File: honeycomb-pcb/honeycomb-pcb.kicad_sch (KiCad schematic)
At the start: 0 parts

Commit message: tmc5130-uart-multiplexer -> honeycomb-pcb
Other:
- title: tmc5130-uart-multiplexer -> honeycomb-pcb
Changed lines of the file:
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@@
   (paper "A4")
   (title_block
-    (title "tmc5130-uart-multiplexer")
+    (title "honeycomb-pcb")
     (date "2024-07-10")
     (rev "1.0")
@@
     )
     (instances
-      (project "tmc5130-uart-multiplexer"
+      (project "honeycomb-pcb"
         (path "/df2b2e89-e055-4140-95de-f1df723db034" (page "2"))
       )
@@
     )
     (instances
-      (project "tmc5130-uart-multiplexer"
+      (project "honeycomb-pcb"
         (path "/df2b2e89-e055-4140-95de-f1df723db034" (page "5"))
       )
@@
     )
     (instances
-      (project "tmc5130-uart-multiplexer"
+      (project "honeycomb-pcb"
         (path "/df2b2e89-e055-4140-95de-f1df723db034" (page "9"))
       )
@@
     )
     (instances
-      (project "tmc5130-uart-multiplexer"
+      (project "honeycomb-pcb"
         (path "/df2b2e89-e055-4140-95de-f1df723db034" (page "11"))
       )
@@
     )
     (instances
-      (project "tmc5130-uart-multiplexer"
+      (project "honeycomb-pcb"
         (path "/df2b2e89-e055-4140-95de-f1df723db034" (page "4"))
       )
@@
     )
     (instances
-      (project "tmc5130-uart-multiplexer"
+      (project "honeycomb-pcb"
         (path "/df2b2e89-e055-4140-95de-f1df723db034" (page "7"))
       )
@@
     )
     (instances
-      (project "tmc5130-uart-multiplexer"
+      (project "honeycomb-pcb"
         (path "/df2b2e89-e055-4140-95de-f1df723db034" (page "6"))
       )
@@
     )
     (instances
-      (project "tmc5130-uart-multiplexer"
+      (project "honeycomb-pcb"
         (path "/df2b2e89-e055-4140-95de-f1df723db034" (page "10"))
       )
@@
     )
     (instances
-      (project "tmc5130-uart-multiplexer"
+      (project "honeycomb-pcb"
         (path "/df2b2e89-e055-4140-95de-f1df723db034" (page "3"))
       )
@@
     )
     (instances
-      (project "tmc5130-uart-multiplexer"
+      (project "honeycomb-pcb"
         (path "/df2b2e89-e055-4140-95de-f1df723db034" (page "8"))
       )

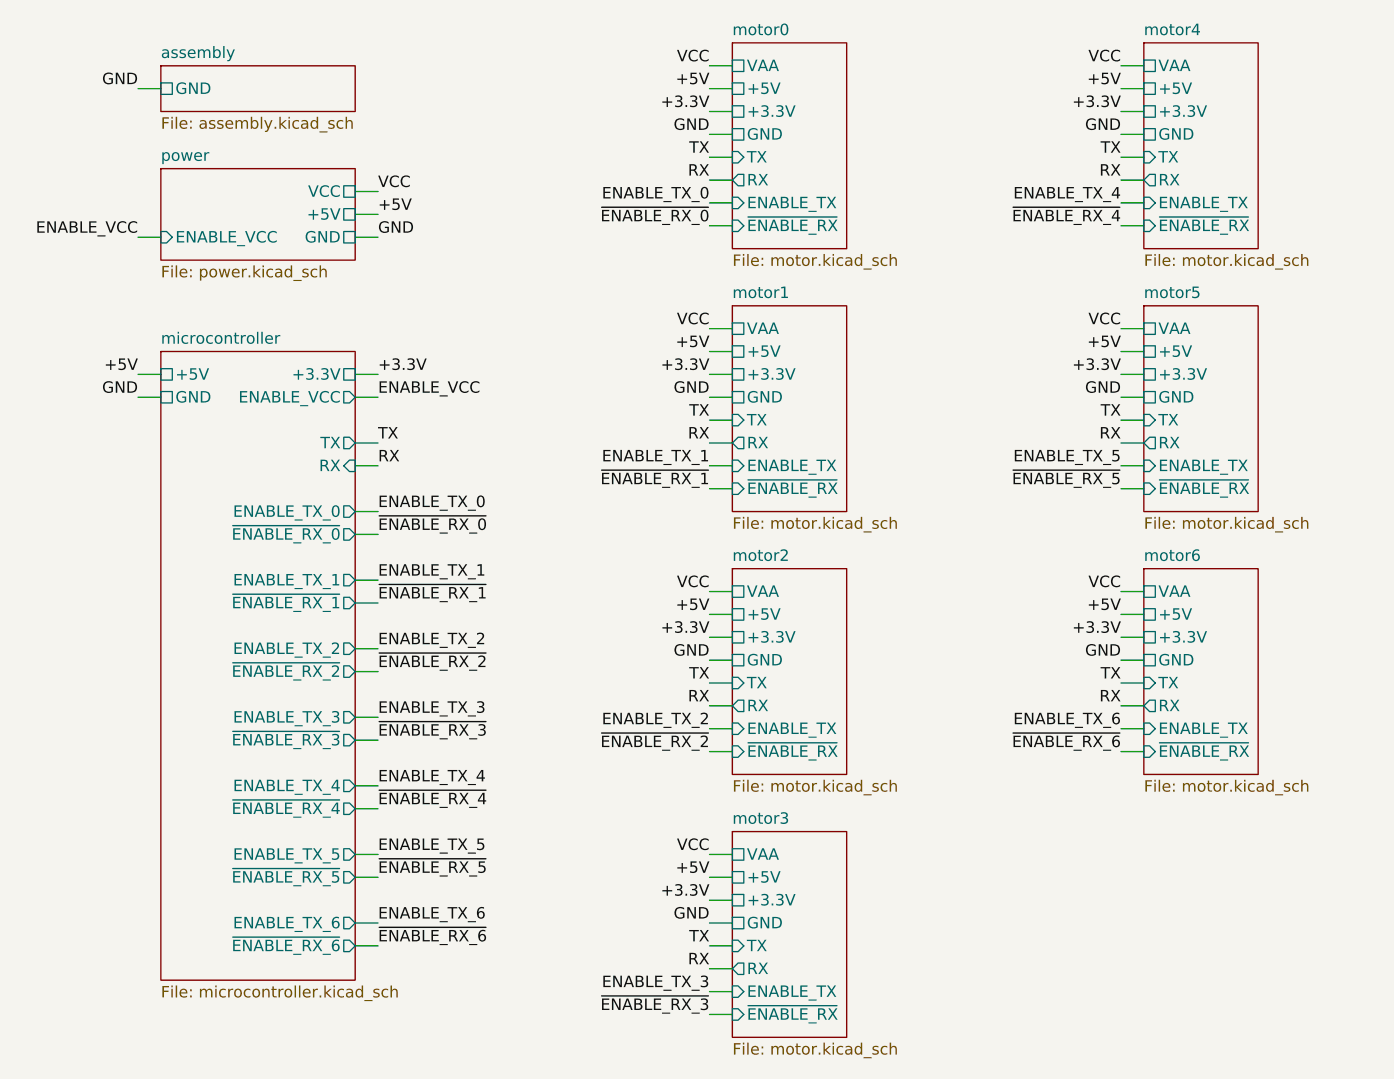
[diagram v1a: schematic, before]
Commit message: motor -> prism
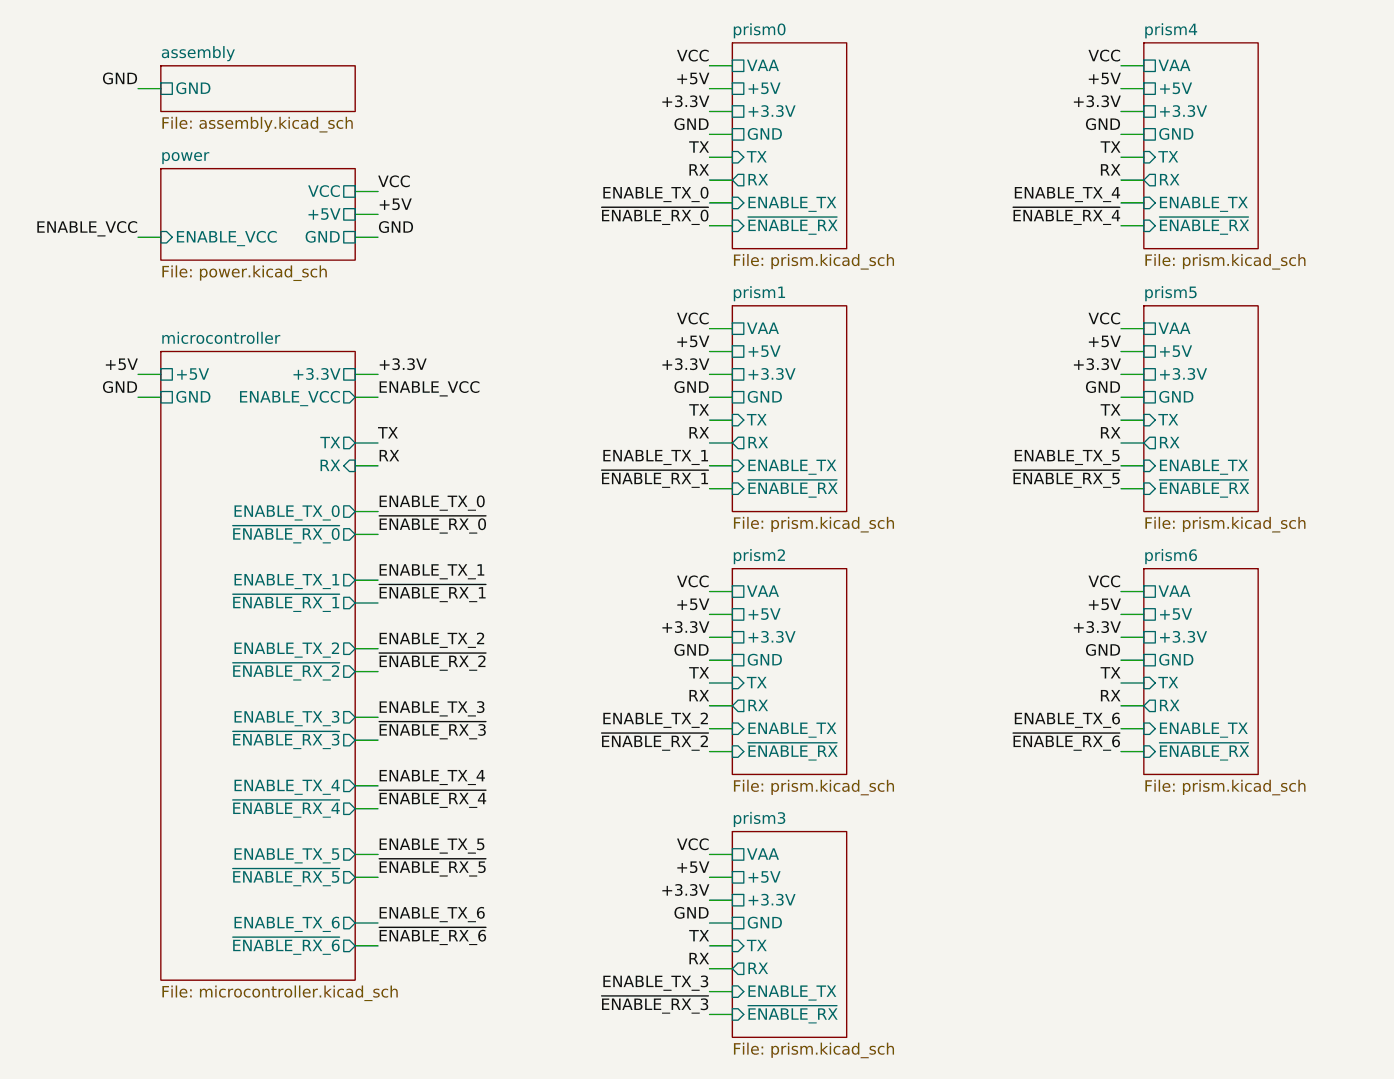
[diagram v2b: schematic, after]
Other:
- sheet motor0 renamed prism0
- sheet motor1 renamed prism1
- sheet motor2 renamed prism2
- sheet motor3 renamed prism3
- sheet motor4 renamed prism4
- sheet motor5 renamed prism5
- sheet motor6 renamed prism6
- sheet prism0: file motor.kicad_sch -> prism.kicad_sch
- sheet prism1: file motor.kicad_sch -> prism.kicad_sch
- sheet prism2: file motor.kicad_sch -> prism.kicad_sch
- sheet prism3: file motor.kicad_sch -> prism.kicad_sch
- sheet prism4: file motor.kicad_sch -> prism.kicad_sch
- sheet prism5: file motor.kicad_sch -> prism.kicad_sch
- sheet prism6: file motor.kicad_sch -> prism.kicad_sch
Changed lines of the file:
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@@
   (title_block
     (title "honeycomb-pcb")
-    (date "2024-07-10")
+    (date "2024-07-12")
     (rev "1.0")
     (company "Howard Hughes Medical Institute")
@@
     (stroke (width 0.1524) (type solid))
     (fill (color 0 0 0 0.0000))
-    (property "Sheetname" "motor0" (at 135.89 48.8184 0)
-      (effects (font (size 1.27 1.27)) (justify left bottom))
-    )
-    (property "Sheetfile" "motor.kicad_sch" (at 135.89 72.9746 0)
+    (property "Sheetname" "prism0" (at 135.89 48.8184 0)
+      (effects (font (size 1.27 1.27)) (justify left bottom))
+    )
+    (property "Sheetfile" "prism.kicad_sch" (at 135.89 72.9746 0)
       (effects (font (size 1.27 1.27)) (justify left top))
     )
@@
     (stroke (width 0.1524) (type solid))
     (fill (color 0 0 0 0.0000))
-    (property "Sheetname" "motor5" (at 181.61 78.0284 0)
-      (effects (font (size 1.27 1.27)) (justify left bottom))
-    )
-    (property "Sheetfile" "motor.kicad_sch" (at 181.61 102.1846 0)
+    (property "Sheetname" "prism5" (at 181.61 78.0284 0)
+      (effects (font (size 1.27 1.27)) (justify left bottom))
+    )
+    (property "Sheetfile" "prism.kicad_sch" (at 181.61 102.1846 0)
       (effects (font (size 1.27 1.27)) (justify left top))
     )
@@
     (stroke (width 0.1524) (type solid))
     (fill (color 0 0 0 0.0000))
-    (property "Sheetname" "motor6" (at 181.61 107.2384 0)
-      (effects (font (size 1.27 1.27)) (justify left bottom))
-    )
-    (property "Sheetfile" "motor.kicad_sch" (at 181.61 131.3946 0)
+    (property "Sheetname" "prism6" (at 181.61 107.2384 0)
+      (effects (font (size 1.27 1.27)) (justify left bottom))
+    )
+    (property "Sheetfile" "prism.kicad_sch" (at 181.61 131.3946 0)
       (effects (font (size 1.27 1.27)) (justify left top))
     )
@@
     (stroke (width 0.1524) (type solid))
     (fill (color 0 0 0 0.0000))
-    (property "Sheetname" "motor2" (at 135.89 107.2384 0)
-      (effects (font (size 1.27 1.27)) (justify left bottom))
-    )
-    (property "Sheetfile" "motor.kicad_sch" (at 135.89 131.3946 0)
+    (property "Sheetname" "prism2" (at 135.89 107.2384 0)
+      (effects (font (size 1.27 1.27)) (justify left bottom))
+    )
+    (property "Sheetfile" "prism.kicad_sch" (at 135.89 131.3946 0)
       (effects (font (size 1.27 1.27)) (justify left top))
     )
@@
     (stroke (width 0.1524) (type solid))
     (fill (color 0 0 0 0.0000))
-    (property "Sheetname" "motor1" (at 135.89 78.0284 0)
-      (effects (font (size 1.27 1.27)) (justify left bottom))
-    )
-    (property "Sheetfile" "motor.kicad_sch" (at 135.89 102.1846 0)
+    (property "Sheetname" "prism1" (at 135.89 78.0284 0)
+      (effects (font (size 1.27 1.27)) (justify left bottom))
+    )
+    (property "Sheetfile" "prism.kicad_sch" (at 135.89 102.1846 0)
       (effects (font (size 1.27 1.27)) (justify left top))
     )
@@
     (stroke (width 0.1524) (type solid))
     (fill (color 0 0 0 0.0000))
-    (property "Sheetname" "motor4" (at 181.61 48.8184 0)
-      (effects (font (size 1.27 1.27)) (justify left bottom))
-    )
-    (property "Sheetfile" "motor.kicad_sch" (at 181.61 72.9746 0)
+    (property "Sheetname" "prism4" (at 181.61 48.8184 0)
+      (effects (font (size 1.27 1.27)) (justify left bottom))
+    )
+    (property "Sheetfile" "prism.kicad_sch" (at 181.61 72.9746 0)
       (effects (font (size 1.27 1.27)) (justify left top))
     )
@@
     (stroke (width 0.1524) (type solid))
     (fill (color 0 0 0 0.0000))
-    (property "Sheetname" "motor3" (at 135.89 136.4484 0)
-      (effects (font (size 1.27 1.27)) (justify left bottom))
-    )
-    (property "Sheetfile" "motor.kicad_sch" (at 135.89 160.6046 0)
-      (effects (font (size 1.27 1.27)) (justify left top))
-    )
+    (property "Sheetname" "prism3" (at 135.89 136.4484 0)
+      (effects (font (size 1.27 1.27)) (justify left bottom))
+    )
+    (property "Sheetfile" "prism.kicad_sch" (at 135.89 160.6046 0)
+      (effects (font (size 1.27 1.27)) (justify left top))
+    )
